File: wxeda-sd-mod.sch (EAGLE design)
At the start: 23 parts, among them U1 SD_CARD, X2 TAPE IN / OUT

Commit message: release
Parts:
- C2, C3, C4, C5: device adafruit:CPOL-USE5-8.5 -> adafruit:CPOL-USE2-5
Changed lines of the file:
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@@
 <part name="R6" library="SparkFun-Passives" deviceset="RESISTOR" device="AXIAL-0.3" value="10k"/>
 <part name="GND5" library="SparkFun-Aesthetics" deviceset="GND" device=""/>
-<part name="C2" library="adafruit" deviceset="CPOL-US" device="E5-8.5" value="10uF"/>
+<part name="C2" library="adafruit" deviceset="CPOL-US" device="E2-5" value="10uF"/>
 <part name="R9" library="SparkFun-Passives" deviceset="RESISTOR" device="AXIAL-0.3" value="75"/>
-<part name="C4" library="adafruit" deviceset="CPOL-US" device="E5-8.5" value="47uF"/>
+<part name="C4" library="adafruit" deviceset="CPOL-US" device="E2-5" value="47uF"/>
 <part name="X2" library="adafruit" deviceset="STEREOJACK" device="" value="TAPE IN / OUT"/>
-<part name="C5" library="adafruit" deviceset="CPOL-US" device="E5-8.5" value="10uF"/>
+<part name="C5" library="adafruit" deviceset="CPOL-US" device="E2-5" value="10uF"/>
 <part name="R7" library="SparkFun-Passives" deviceset="RESISTOR" device="AXIAL-0.3" value="75"/>
-<part name="C3" library="adafruit" deviceset="CPOL-US" device="E5-8.5" value="47uF"/>
+<part name="C3" library="adafruit" deviceset="CPOL-US" device="E2-5" value="47uF"/>
 <part name="U$1" library="connectors-digital" deviceset="MINIDIN_4" device="" value="S-VIDEO"/>
 <part name="GND6" library="SparkFun-Aesthetics" deviceset="GND" device=""/>

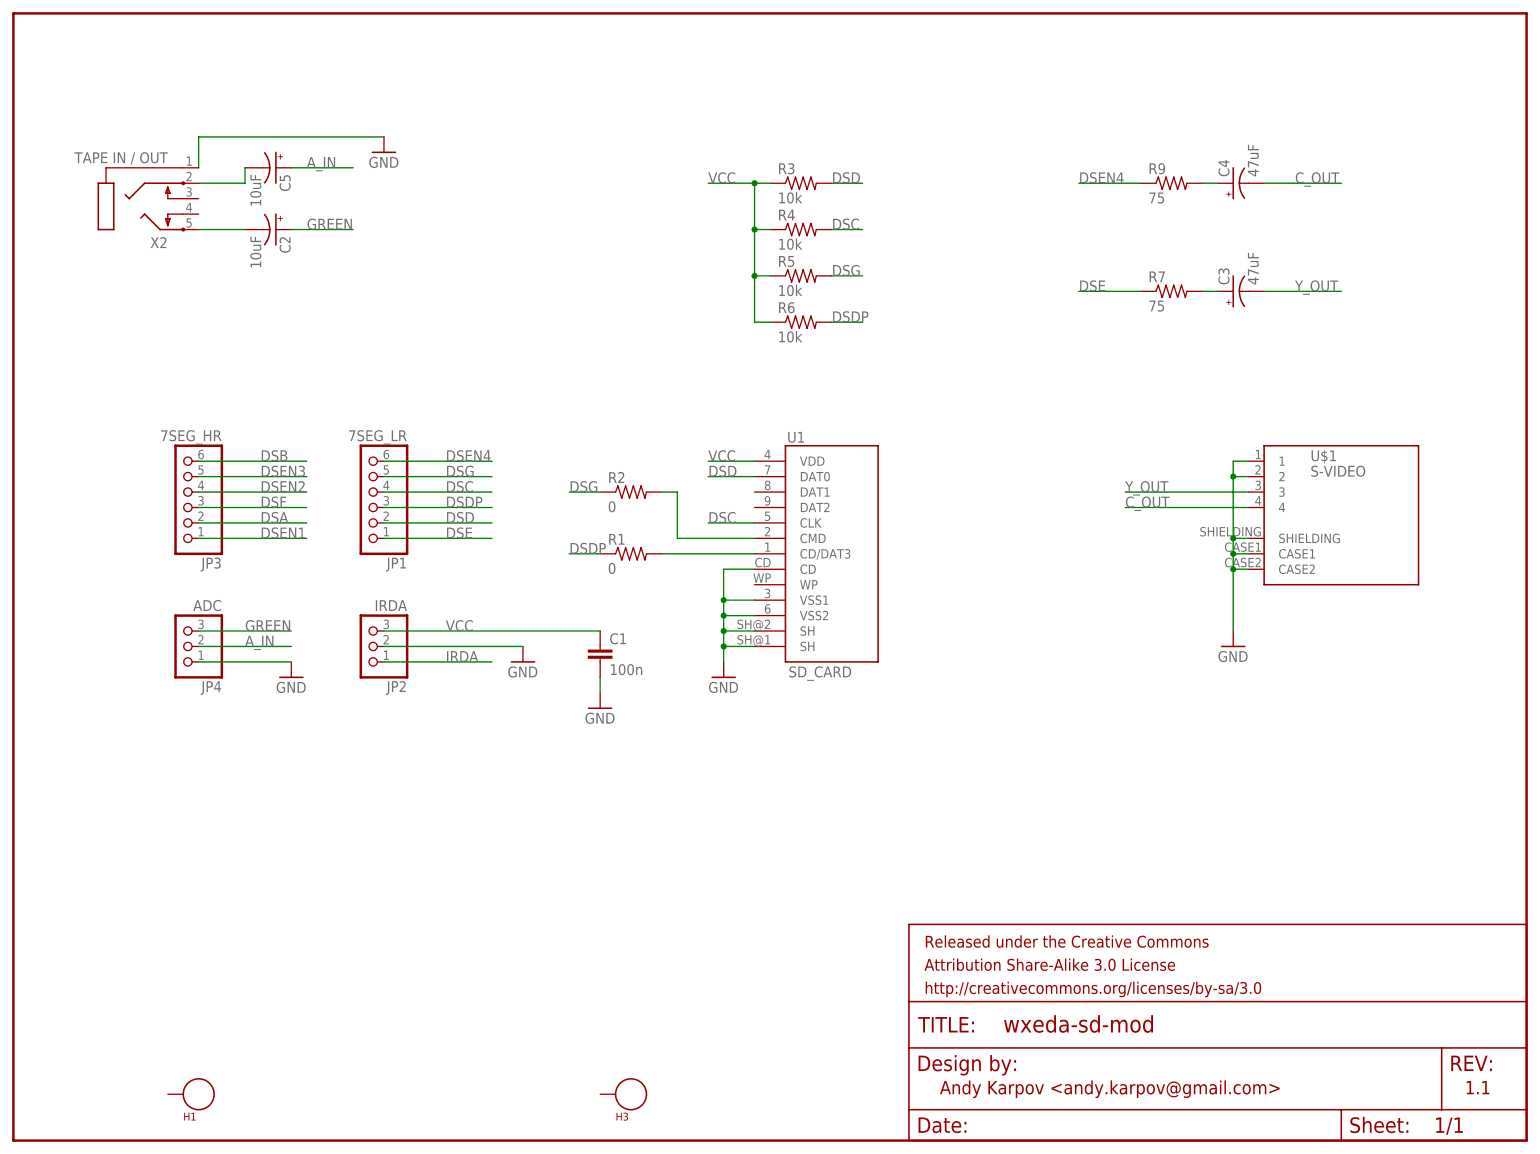
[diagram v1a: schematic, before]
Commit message: Added stereo output
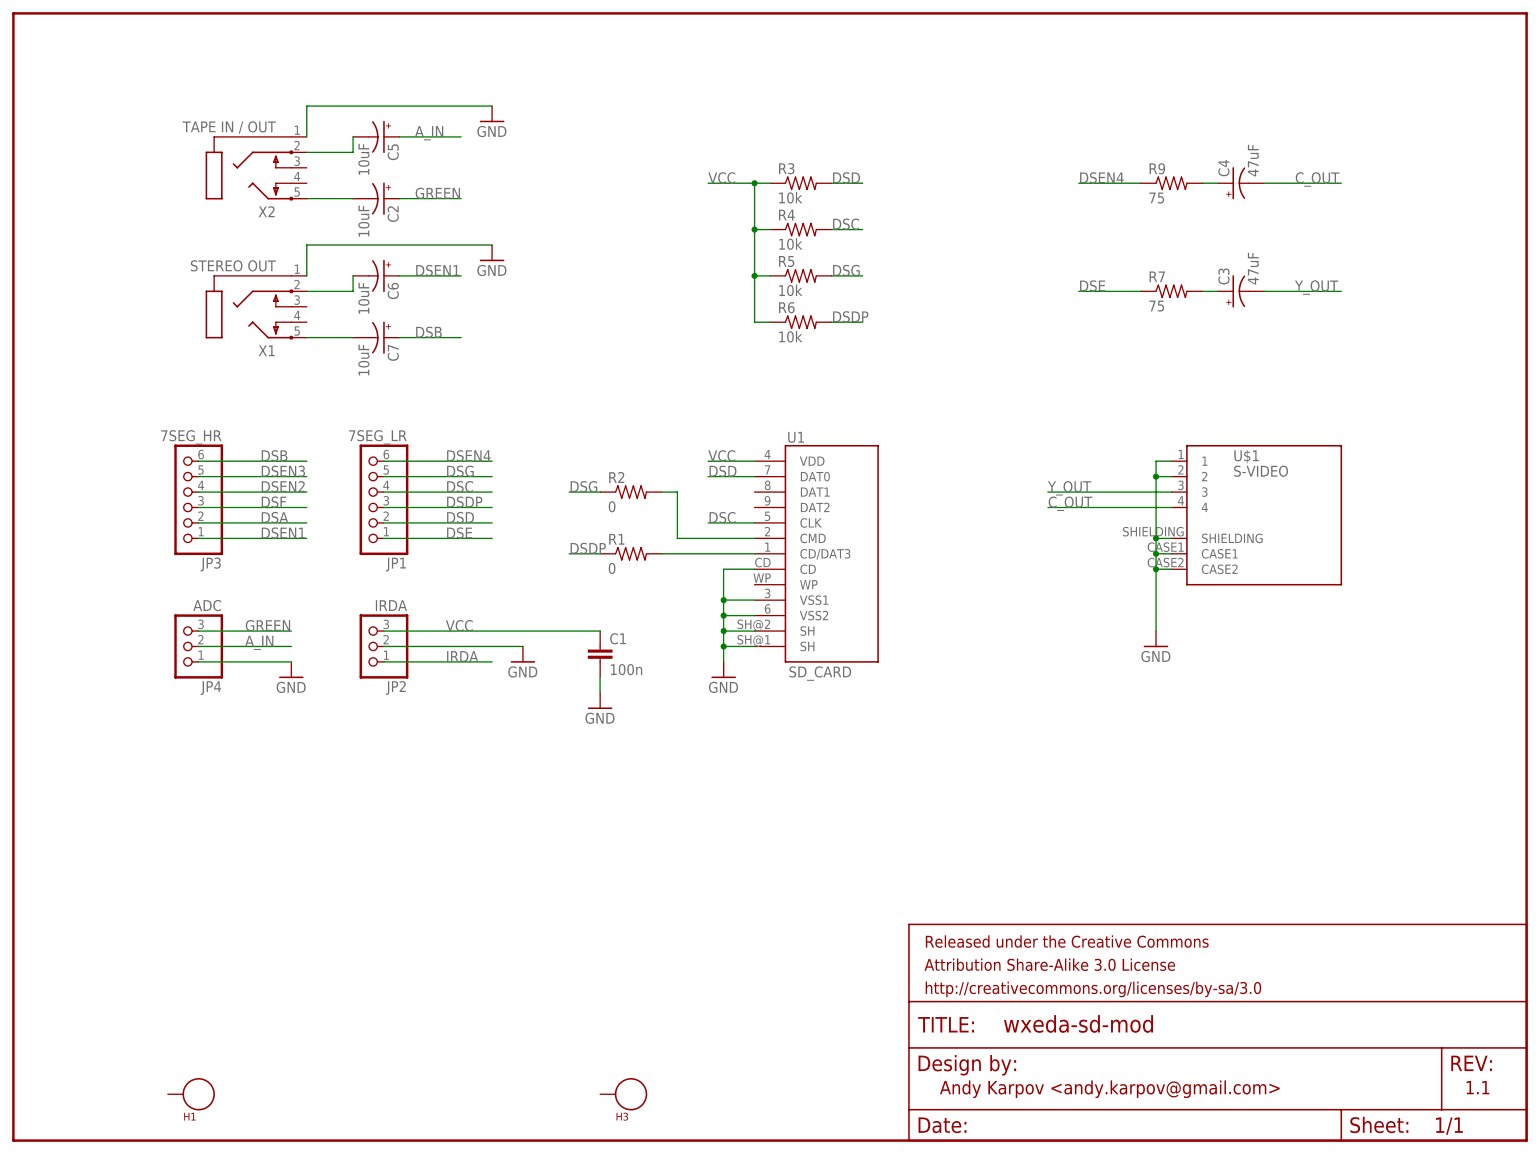
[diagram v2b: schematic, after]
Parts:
- added C6, C7: 10uF, adafruit:CPOL-USE2-5
- added X1: STEREO OUT, adafruit:STEREOJACK
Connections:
- new net N$10: C7.-, X1.5
- new net N$5: C6.-, X1.2
- net DSB: now also C7.+
- net DSEN1: now also C6.+
- net GND: now also X1.1
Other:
- moved on the sheet: C2, C5, U$1, X2
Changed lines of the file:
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@@
 <part name="U$1" library="connectors-digital" deviceset="MINIDIN_4" device="" value="S-VIDEO"/>
 <part name="GND6" library="SparkFun-Aesthetics" deviceset="GND" device=""/>
+<part name="X1" library="adafruit" deviceset="STEREOJACK" device="" value="STEREO OUT"/>
+<part name="C6" library="adafruit" deviceset="CPOL-US" device="E2-5" value="10uF"/>
+<part name="C7" library="adafruit" deviceset="CPOL-US" device="E2-5" value="10uF"/>
+<part name="GND7" library="SparkFun-Aesthetics" deviceset="GND" device=""/>
 </parts>
 <sheets>
@@
 <instance part="R5" gate="G$1" x="129.54" y="142.24"/>
 <instance part="R6" gate="G$1" x="129.54" y="134.62"/>
-<instance part="GND5" gate="1" x="60.96" y="162.56"/>
-<instance part="C2" gate="G$1" x="43.18" y="149.86" rot="R270"/>
+<instance part="GND5" gate="1" x="78.74" y="167.64"/>
+<instance part="C2" gate="G$1" x="60.96" y="154.94" rot="R270"/>
 <instance part="R9" gate="G$1" x="190.5" y="157.48"/>
 <instance part="C4" gate="G$1" x="200.66" y="157.48" rot="R90"/>
-<instance part="X2" gate="1" x="17.78" y="152.4" rot="R180"/>
-<instance part="C5" gate="G$1" x="43.18" y="160.02" rot="R270"/>
+<instance part="X2" gate="1" x="35.56" y="157.48" rot="R180"/>
+<instance part="C5" gate="G$1" x="60.96" y="165.1" rot="R270"/>
 <instance part="R7" gate="G$1" x="190.5" y="139.7"/>
 <instance part="C3" gate="G$1" x="200.66" y="139.7" rot="R90"/>
-<instance part="U$1" gate="G$1" x="218.44" y="101.6"/>
-<instance part="GND6" gate="1" x="200.66" y="81.28"/>
+<instance part="U$1" gate="G$1" x="205.74" y="101.6"/>
+<instance part="GND6" gate="1" x="187.96" y="81.28"/>
+<instance part="X1" gate="1" x="35.56" y="134.62" rot="R180"/>
+<instance part="C6" gate="G$1" x="60.96" y="142.24" rot="R270"/>
+<instance part="C7" gate="G$1" x="60.96" y="132.08" rot="R270"/>
+<instance part="GND7" gate="1" x="78.74" y="144.78"/>
 </instances>
 <busses>
@@
 <pinref part="X2" gate="1" pin="1"/>
 <pinref part="GND5" gate="1" pin="GND"/>
-<wire x1="30.48" y1="160.02" x2="30.48" y2="165.1" width="0.1524" layer="91"/>
-<wire x1="30.48" y1="165.1" x2="60.96" y2="165.1" width="0.1524" layer="91"/>
+<wire x1="48.26" y1="165.1" x2="48.26" y2="170.18" width="0.1524" layer="91"/>
+<wire x1="48.26" y1="170.18" x2="78.74" y2="170.18" width="0.1524" layer="91"/>
 </segment>
 <segment>
 <pinref part="U$1" gate="G$1" pin="SHIELDING"/>
-<wire x1="203.2" y1="99.06" x2="200.66" y2="99.06" width="0.1524" layer="91"/>
-<wire x1="200.66" y1="99.06" x2="200.66" y2="96.52" width="0.1524" layer="91"/>
+<wire x1="190.5" y1="99.06" x2="187.96" y2="99.06" width="0.1524" layer="91"/>
+<wire x1="187.96" y1="99.06" x2="187.96" y2="96.52" width="0.1524" layer="91"/>
 <pinref part="U$1" gate="G$1" pin="CASE1"/>
-<wire x1="200.66" y1="96.52" x2="200.66" y2="93.98" width="0.1524" layer="91"/>
-<wire x1="200.66" y1="93.98" x2="200.66" y2="83.82" width="0.1524" layer="91"/>
-<wire x1="203.2" y1="96.52" x2="200.66" y2="96.52" width="0.1524" layer="91"/>
-<junction x="200.66" y="96.52"/>
+<wire x1="187.96" y1="96.52" x2="187.96" y2="93.98" width="0.1524" layer="91"/>
+<wire x1="187.96" y1="93.98" x2="187.96" y2="83.82" width="0.1524" layer="91"/>
+<wire x1="190.5" y1="96.52" x2="187.96" y2="96.52" width="0.1524" layer="91"/>
+<junction x="187.96" y="96.52"/>
 <pinref part="U$1" gate="G$1" pin="CASE2"/>
-<wire x1="203.2" y1="93.98" x2="200.66" y2="93.98" width="0.1524" layer="91"/>
-<junction x="200.66" y="93.98"/>
+<wire x1="190.5" y1="93.98" x2="187.96" y2="93.98" width="0.1524" layer="91"/>
+<junction x="187.96" y="93.98"/>
 <pinref part="GND6" gate="1" pin="GND"/>
 <pinref part="U$1" gate="G$1" pin="1"/>
-<wire x1="203.2" y1="111.76" x2="200.66" y2="111.76" width="0.1524" layer="91"/>
-<wire x1="200.66" y1="111.76" x2="200.66" y2="109.22" width="0.1524" layer="91"/>
-<junction x="200.66" y="99.06"/>
+<wire x1="190.5" y1="111.76" x2="187.96" y2="111.76" width="0.1524" layer="91"/>
+<wire x1="187.96" y1="111.76" x2="187.96" y2="109.22" width="0.1524" layer="91"/>
+<junction x="187.96" y="99.06"/>
 <pinref part="U$1" gate="G$1" pin="2"/>
-<wire x1="200.66" y1="109.22" x2="200.66" y2="99.06" width="0.1524" layer="91"/>
-<wire x1="203.2" y1="109.22" x2="200.66" y2="109.22" width="0.1524" layer="91"/>
-<junction x="200.66" y="109.22"/>
+<wire x1="187.96" y1="109.22" x2="187.96" y2="99.06" width="0.1524" layer="91"/>
+<wire x1="190.5" y1="109.22" x2="187.96" y2="109.22" width="0.1524" layer="91"/>
+<junction x="187.96" y="109.22"/>
+</segment>
+<segment>
+<pinref part="X1" gate="1" pin="1"/>
+<wire x1="48.26" y1="142.24" x2="48.26" y2="147.32" width="0.1524" layer="91"/>
+<pinref part="GND7" gate="1" pin="GND"/>
+<wire x1="48.26" y1="147.32" x2="78.74" y2="147.32" width="0.1524" layer="91"/>
 </segment>
 </net>
@@
 <label x="40.64" y="111.76" size="1.778" layer="95"/>
 </segment>
+<segment>
+<pinref part="C7" gate="G$1" pin="+"/>
+<wire x1="63.5" y1="132.08" x2="73.66" y2="132.08" width="0.1524" layer="91"/>
+<label x="66.04" y="132.08" size="1.778" layer="95"/>
+</segment>
 </net>
 <net name="DSEN3" class="0">
@@
 <label x="40.64" y="99.06" size="1.778" layer="95"/>
 </segment>
+<segment>
+<pinref part="C6" gate="G$1" pin="+"/>
+<wire x1="63.5" y1="142.24" x2="73.66" y2="142.24" width="0.1524" layer="91"/>
+<label x="66.04" y="142.24" size="1.778" layer="95"/>
+</segment>
 </net>
 <net name="A_IN" class="0">
@@
 </segment>
 <segment>
-<wire x1="45.72" y1="160.02" x2="55.88" y2="160.02" width="0.1524" layer="91"/>
-<label x="48.26" y="160.02" size="1.778" layer="95"/>
+<wire x1="63.5" y1="165.1" x2="73.66" y2="165.1" width="0.1524" layer="91"/>
+<label x="66.04" y="165.1" size="1.778" layer="95"/>
 <pinref part="C5" gate="G$1" pin="+"/>
 </segment>
@@
 <segment>
 <pinref part="C2" gate="G$1" pin="+"/>
-<wire x1="45.72" y1="149.86" x2="55.88" y2="149.86" width="0.1524" layer="91"/>
-<label x="48.26" y="149.86" size="1.778" layer="95"/>
+<wire x1="63.5" y1="154.94" x2="73.66" y2="154.94" width="0.1524" layer="91"/>
+<label x="66.04" y="154.94" size="1.778" layer="95"/>
 </segment>
 </net>
@@
 <pinref part="X2" gate="1" pin="5"/>
 <pinref part="C2" gate="G$1" pin="-"/>
-<wire x1="30.48" y1="149.86" x2="38.1" y2="149.86" width="0.1524" layer="91"/>
+<wire x1="48.26" y1="154.94" x2="55.88" y2="154.94" width="0.1524" layer="91"/>
 </segment>
 </net>
@@
 <pinref part="X2" gate="1" pin="2"/>
 <pinref part="C5" gate="G$1" pin="-"/>
-<wire x1="30.48" y1="157.48" x2="38.1" y2="157.48" width="0.1524" layer="91"/>
-<wire x1="38.1" y1="157.48" x2="38.1" y2="160.02" width="0.1524" layer="91"/>
+<wire x1="48.26" y1="162.56" x2="55.88" y2="162.56" width="0.1524" layer="91"/>
+<wire x1="55.88" y1="162.56" x2="55.88" y2="165.1" width="0.1524" layer="91"/>
 </segment>
 </net>
@@
 <segment>
 <pinref part="U$1" gate="G$1" pin="3"/>
-<wire x1="203.2" y1="106.68" x2="182.88" y2="106.68" width="0.1524" layer="91"/>
-<label x="182.88" y="106.68" size="1.778" layer="95"/>
+<wire x1="190.5" y1="106.68" x2="170.18" y2="106.68" width="0.1524" layer="91"/>
+<label x="170.18" y="106.68" size="1.778" layer="95"/>
 </segment>
 <segment>
@@
 <segment>
 <pinref part="U$1" gate="G$1" pin="4"/>
-<wire x1="203.2" y1="104.14" x2="182.88" y2="104.14" width="0.1524" layer="91"/>
-<label x="182.88" y="104.14" size="1.778" layer="95"/>
+<wire x1="190.5" y1="104.14" x2="170.18" y2="104.14" width="0.1524" layer="91"/>
+<label x="170.18" y="104.14" size="1.778" layer="95"/>
 </segment>
 <segment>
@@
 </segment>
 </net>
+<net name="N$5" class="0">
+<segment>
+<pinref part="X1" gate="1" pin="2"/>
+<wire x1="48.26" y1="139.7" x2="55.88" y2="139.7" width="0.1524" layer="91"/>
+<pinref part="C6" gate="G$1" pin="-"/>
+<wire x1="55.88" y1="139.7" x2="55.88" y2="142.24" width="0.1524" layer="91"/>
+</segment>
+</net>
+<net name="N$10" class="0">
+<segment>
+<pinref part="X1" gate="1" pin="5"/>
+<pinref part="C7" gate="G$1" pin="-"/>
+<wire x1="48.26" y1="132.08" x2="55.88" y2="132.08" width="0.1524" layer="91"/>
+</segment>
+</net>
